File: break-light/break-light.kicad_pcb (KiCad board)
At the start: 2 copper layers, 70 x 70 mm, 78 parts, among them J1 Conn_01x03, J10 Conn_01x08, J11 Conn_01x08, J13 Conn_01x08, J14 Conn_01x08, J15 Conn_01x08, J16 Conn_01x08, J17 Conn_01x08, J3 Conn_01x05, J4 Conn_01x05, J9 Conn_01x08, SW1 SW_SPST, SW2 SW_SPST, U1 STM32F103C8Tx, U2 SN65HVD256D, U4 AP2204K-ADJ, U5 AP63200WU, U6 MAX7219CNG, U7 MAX7219CNG, U8 MAX7219CNG, U9 MAX7219CNG, Y1 8M, Y2 32.768k

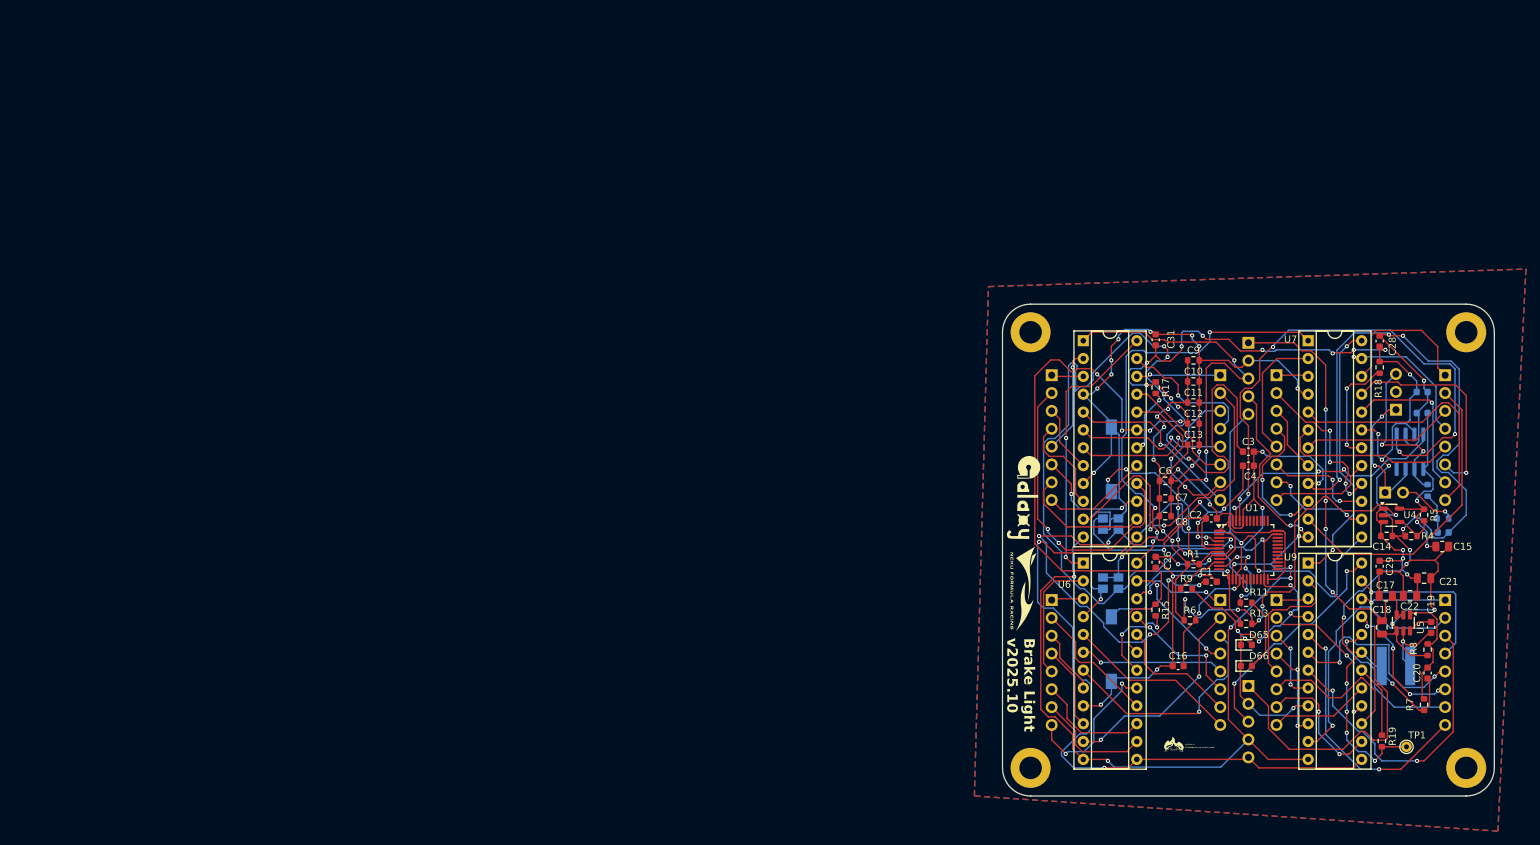
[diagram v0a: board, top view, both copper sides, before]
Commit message: fix: re-layout with 4 layers board
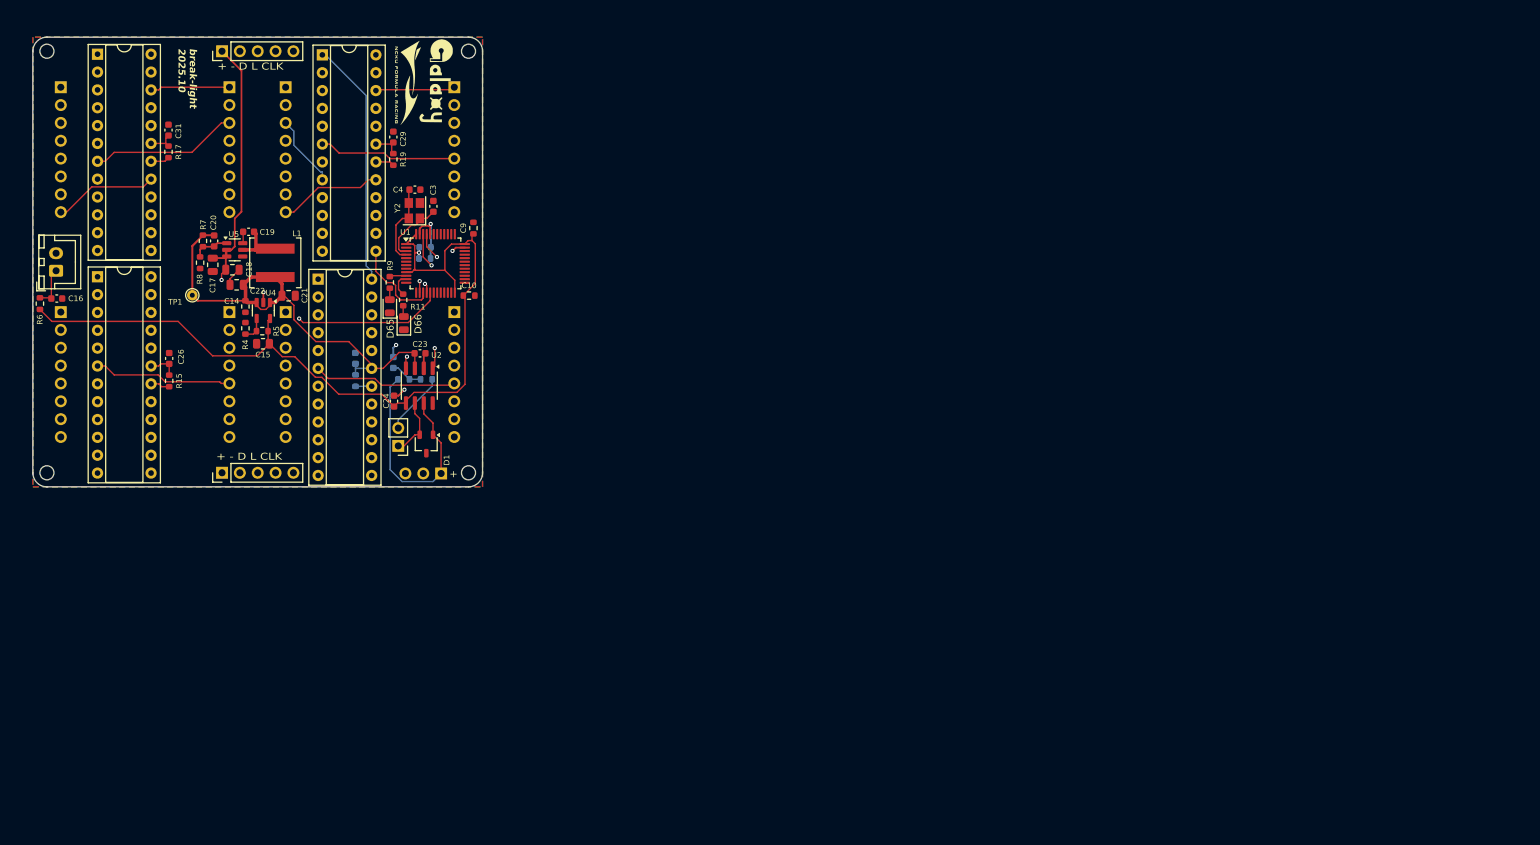
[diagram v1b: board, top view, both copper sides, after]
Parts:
- removed C1, C2: 20p, Capacitor_SMD:C_0603_1608Metric
- removed C12, C6, C8: 100n, Resistor_SMD:R_0603_1608Metric
- removed C7: 1u, Resistor_SMD:R_0603_1608Metric
- removed G***: LOGO, graph:shark
- removed H1, H2, H3, H4: MountingHole_Pad, MountingHole:MountingHole_3.2mm_M3_ISO7380_Pad
- removed R1, R13: 10k, Resistor_SMD:R_0603_1608Metric
- removed SW1, SW2: SW_SPST, Button_Switch_SMD:SW_SPST_FSMSM
- removed Y1: 8M, Crystal:Crystal_SMD_SeikoEpson_FA238-4Pin_3.2x2.5mm
- added D1: DESD2CAN2SOQ, Package_TO_SOT_SMD:TSOT-23, F.Cu at (75.0, 76.9)
- added J2: BSPD_IN, Connector_JST:JST_XH_B2B-XH-A_1x02_P2.50mm_Vertical, F.Cu at (22.3, 52.2)
- C11, C13, C28, R18: moved to B.Cu
- C23, C24, J3, J4, JP1, L1, U2, Y2: moved to F.Cu
- D65, D66: footprint LED_SMD:LED_0603_1608Metric -> LED_SMD:LED_0805_2012Metric
- moved R7 185.9 mm to (43.2, 48.0), turned to -90 degrees
- moved TP1 184.4 mm to (41.7, 55.7)
- moved C20 183.3 mm to (44.8, 48.0), turned to -90 degrees
- moved R8 183.2 mm to (42.8, 51.1)
- moved C19 177.5 mm to (49.7, 46.7), turned to 180 degrees
- moved U5 174.6 mm to (47.7, 49.3), turned to 0 degrees
- moved C17 173.5 mm to (44.6, 51.4), turned to -90 degrees
- moved C22 172.8 mm to (48.0, 54.2)
- moved J4 171.8 mm to (45.9, 21.0), turned to 90 degrees
- moved C18 171.3 mm to (47.4, 52.1), turned to 0 degrees
- moved C15 170.3 mm to (51.8, 62.6), turned to 180 degrees
- moved R6 169.8 mm to (20.0, 56.9), turned to 90 degrees
- moved L1 169.5 mm to (53.5, 51.1), turned to -90 degrees
- moved R4 168.5 mm to (49.2, 60.4), turned to -90 degrees
- moved C16 168.0 mm to (22.4, 56.2), turned to 180 degrees
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- renumbered G*** to G1, G*** to G2
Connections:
- JP1 pad 1: CAN+ -> CAN-
- R3 pad 2: CAN- -> CAN+
- U1 pad 1: +3.3V -> +3V3
- U1 pad 13: Net-(SW2-A) -> unconnected-(U1-PA3-Pad13)
- U1 pad 24: +3.3V -> +3V3
- U1 pad 36: +3.3V -> +3V3
- U1 pad 48: +3.3V -> +3V3
- U1 pad 5: /RCC_OSC_IN -> unconnected-(U1-PD0-Pad5)
- U1 pad 6: /RCC_OSC_OUT -> unconnected-(U1-PD1-Pad6)
- U1 pad 7: Net-(SW1-B) -> unconnected-(U1-NRST-Pad7)
- U1 pad 9: +3.3V -> +3V3
- U2 pad 8: unconnected-(U2-S-Pad8) -> GND
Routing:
- net GND: track 446.7 -> 21.1 mm, vias 38 -> 5
- net /LSE_IN: track 142.3 -> 9.46 mm, vias 4 -> 0
- net +5V: track 275.1 -> 160.6 mm, vias 28 -> 0
- net /RCC_OSC_IN: track 69.0 -> 0.00 mm, vias 6 -> 0
- net CAN_TX: track 79.7 -> 19.9 mm, vias 5 -> 2
- net BSPD_IN: track 17.3 -> 61.9 mm, vias 2 -> 1
- net DOUT2: track 62.6 -> 25.2 mm, vias 4 -> 0
- net VDC: track 106.8 -> 71.6 mm, vias 4 -> 1
- net Net-(SW2-A): track 29.5 -> 0.00 mm, vias 1 -> 0
- net /RCC_OSC_OUT: track 29.2 -> 0.00 mm, vias 1 -> 0
- net Net-(SW1-B): track 28.9 -> 0.00 mm, vias 3 -> 0
- net /LSE_OUT: track 39.1 -> 11.7 mm, vias 6 -> 0
- net +3.3V: track 26.9 -> 0.00 mm
- net COL1_1: track 43.7 -> 19.3 mm, vias 2 -> 0
- net DIN: track 78.3 -> 102.4 mm, vias 7 -> 1
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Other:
- board size 70 x 70 mm -> 64 x 64 mm
- copper layers 2 -> 4
- board text added: "+"
- board text added: "+ - D L CLK"
- board text added: "break-light 2025.10"
- board text removed: "Brake Light v2025.10"

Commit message: v2025.10
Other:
- board text added: "brake-light 2025.10"
- board text removed: "break-light 2025.10"
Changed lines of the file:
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@@
     (effects (font (size 1 1) (thickness 0.1)) (justify left bottom))
   )
-  (gr_text "break-light\n2025.10" (at 39.6 20.6 -90) (layer "F.SilkS")
+  (gr_text "brake-light\n2025.10" (at 39.6 20.6 270) (layer "F.SilkS")
     (effects (font (size 1 1) (thickness 0.2) bold italic) (justify left bottom))
   )

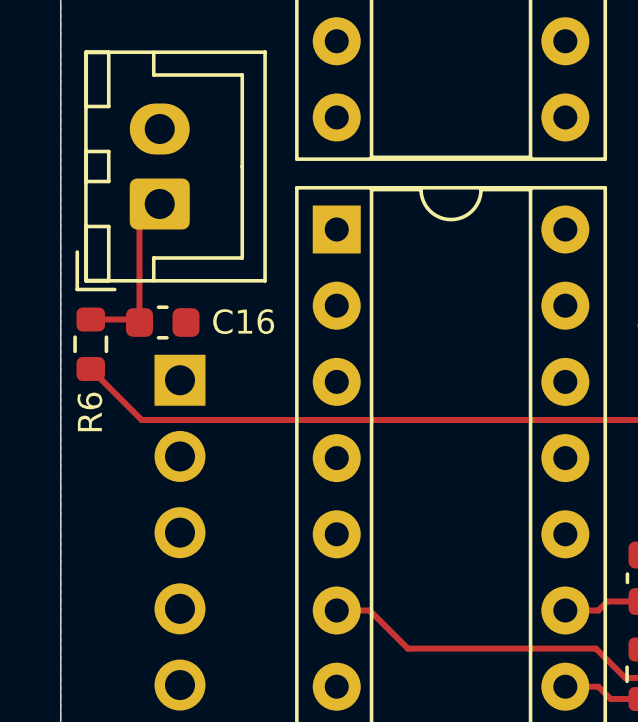
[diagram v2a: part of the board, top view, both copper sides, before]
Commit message: feat: add RC filter for brake light
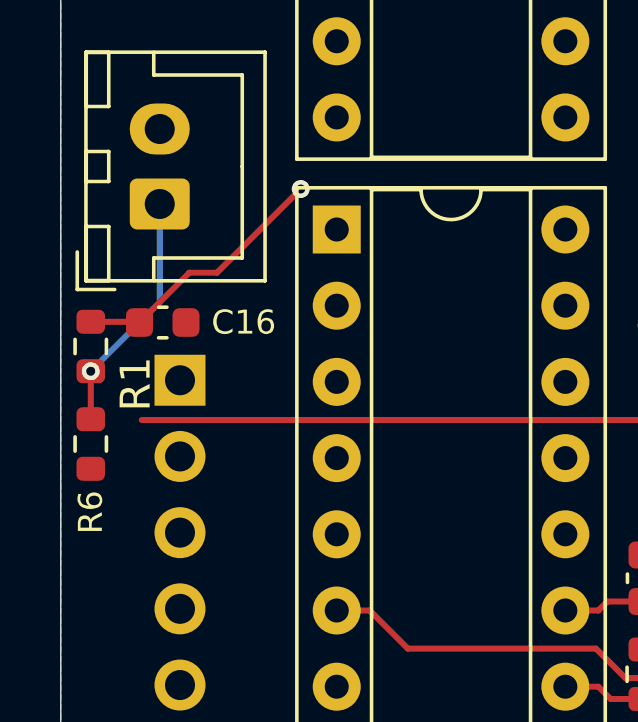
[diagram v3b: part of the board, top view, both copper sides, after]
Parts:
- added R1: 10k, Resistor_SMD:R_0603_1608Metric, F.Cu at (20.0, 57.0)
- moved R6 3.33 mm to (20.0, 60.2)
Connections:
- C16 pad 2: BSPD_IN -> Net-(U1-PA6)
- J2 pad 1: BSPD_IN -> BSE_IN
- R6 pad 1: +3V3 -> GND
- R6 pad 2: BSPD_IN -> BSE_IN
- U1 pad 16: BSPD_IN -> Net-(U1-PA6)
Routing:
- net BSPD_IN: track 61.9 -> 0.00 mm, vias 1 -> 0
- net Net-(U1-PA6): track 0.00 -> 59.3 mm, vias 0 -> 2
- net BSE_IN: track 0.00 -> 9.08 mm, vias 0 -> 1
- net +3V3: track 121.2 -> 118.8 mm

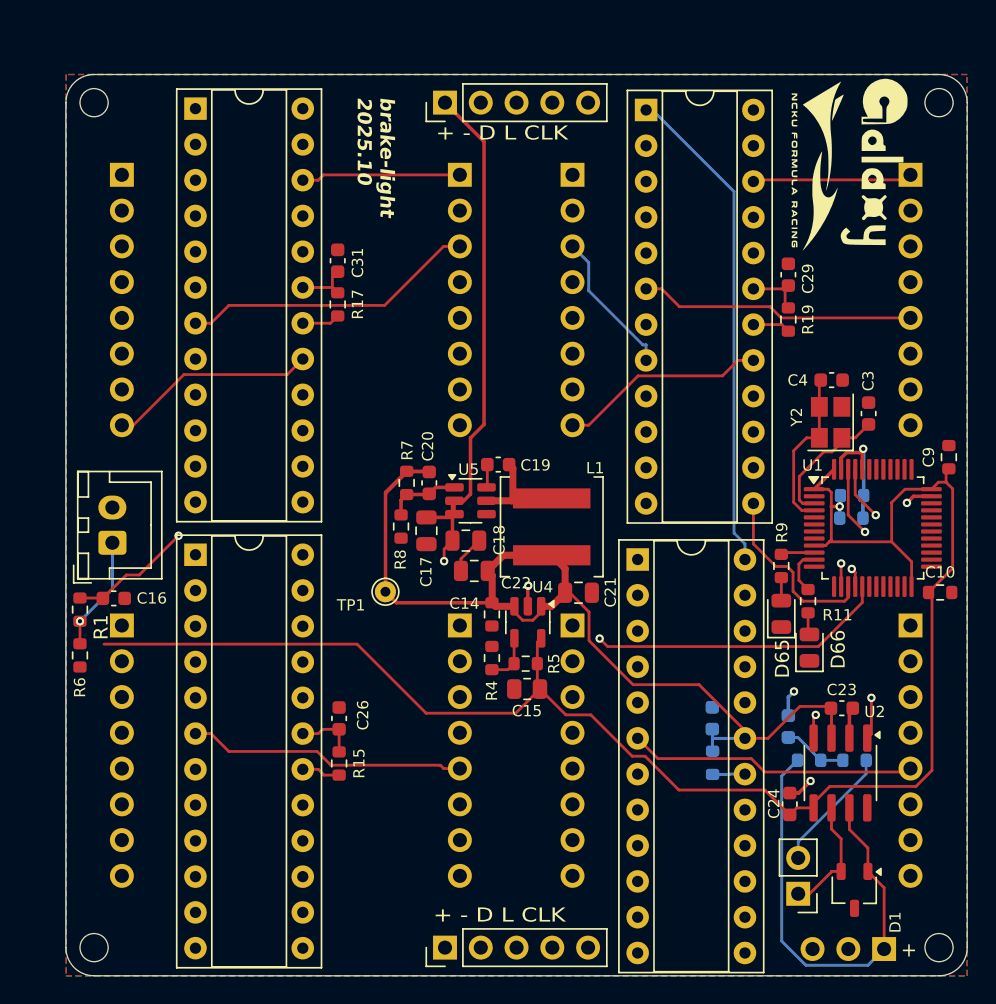
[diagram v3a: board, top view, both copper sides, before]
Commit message: feat: flip one side of the LED matrix
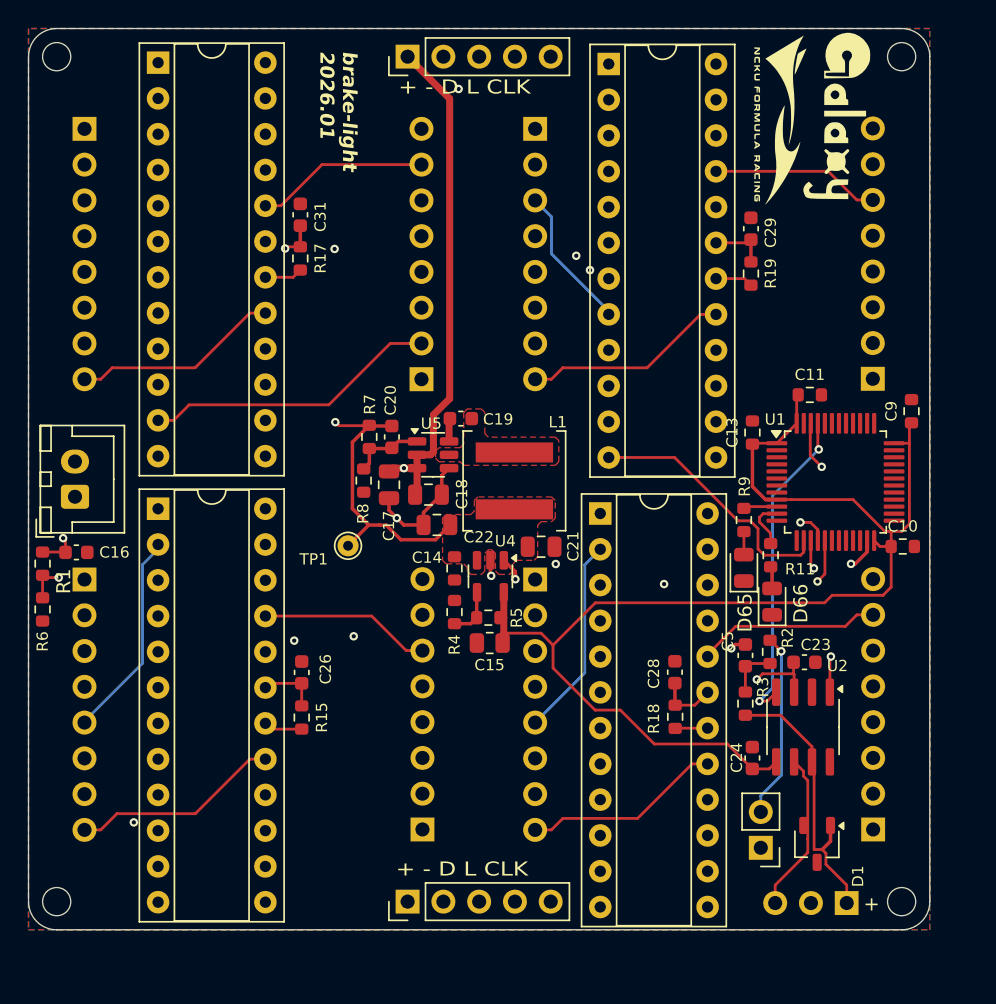
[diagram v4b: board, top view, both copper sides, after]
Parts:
- removed C3, C4: 20p, Capacitor_SMD:C_0603_1608Metric
- removed Y2: 32.768k, Crystal:Crystal_SMD_SeikoEpson_FA238-4Pin_3.2x2.5mm
- C11, C13, C28, C5, R18, R2, R3: moved to F.Cu
- moved J14 14.8 mm to (44.2, 40.6), turned to 0 degrees
- moved J17 14.7 mm to (76.3, 40.6), turned to 0 degrees
- moved J15 14.7 mm to (44.3, 72.6), turned to 0 degrees
- moved J16 14.7 mm to (76.3, 72.6), turned to 0 degrees
- moved R2 9.76 mm to (69.0, 60.0), turned to -90 degrees
- moved C13 9.29 mm to (67.8, 44.4), turned to 90 degrees
- moved C11 7.75 mm to (71.8, 41.8)
- moved R3 6.06 mm to (67.2, 63.7), turned to -90 degrees
- moved C5 5.90 mm to (67.2, 60.2)
- moved C29 4.21 mm to (67.6, 29.9)
- moved C10 4.21 mm to (78.4, 52.5)
- moved C14 4.21 mm to (46.6, 54.1)
- moved C15 4.21 mm to (49.1, 59.4)
- moved C17 4.21 mm to (41.9, 48.1)
- moved C18 4.21 mm to (44.7, 48.8)
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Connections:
- U1 pad 3: /LSE_IN -> unconnected-(U1-PC14-Pad3)
- U1 pad 4: /LSE_OUT -> unconnected-(U1-PC15-Pad4)
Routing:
- net +5V: track 160.6 -> 129.6 mm, vias 0 -> 10
- net +3V3: track 118.8 -> 89.5 mm, vias 1 -> 0
- net ROW1_1: track 38.1 -> 21.0 mm
- net ROW4_1: track 38.3 -> 22.0 mm
- net CAN+: track 32.8 -> 20.1 mm
- net /LSE_OUT: track 11.7 -> 0.00 mm
- net COL2_7: track 11.4 -> 22.5 mm
- net COL1_7: track 11.3 -> 22.2 mm
- net COL4_7: track 11.4 -> 21.9 mm
- net COL3_7: track 11.9 -> 22.2 mm
- net DIN: track 102.4 -> 112.1 mm, vias 1 -> 3
- net /LSE_IN: track 9.46 -> 0.00 mm
- net ROW1_2: track 28.1 -> 19.5 mm
- net GND: track 21.1 -> 13.1 mm, vias 5 -> 4
- net ROW3_1: track 30.4 -> 22.6 mm
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- added copper zone on F.Cu, net +5V
- added copper zone on F.Cu, net Net-(U5-SW)
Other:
- board text added: "brake-light 2026.01"
- board text removed: "brake-light 2025.10"

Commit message: fix: repair pin
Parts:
- added J5: Conn_01x03, Connector_PinHeader_2.54mm:PinHeader_1x03_P2.54mm_Vertical, F.Cu at (72.0, 36.6)
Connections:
- J10 pad 1: ROW3_4 -> COL3_7
- J10 pad 2: COL3_1 -> COL3_6
- J10 pad 3: ROW3_7 -> ROW3_1
- J10 pad 4: ROW3_5 -> COL3_0
- J10 pad 5: ROW3_0 -> ROW3_3
- J10 pad 7: COL3_0 -> COL3_3
- J10 pad 8: COL3_6 -> ROW3_0
- J11 pad 1: ROW4_4 -> COL4_7
- J11 pad 2: COL4_1 -> COL4_6
- J11 pad 3: ROW4_7 -> ROW4_1
- J11 pad 4: ROW4_5 -> COL4_0
- J11 pad 5: ROW4_0 -> ROW4_3
- J11 pad 7: COL4_0 -> COL4_3
- J11 pad 8: COL4_6 -> ROW4_0
- J13 pad 1: ROW1_4 -> COL1_7
- J13 pad 2: COL1_1 -> COL1_6
- J13 pad 3: ROW1_7 -> ROW1_1
- J13 pad 4: ROW1_5 -> COL1_0
- J13 pad 5: ROW1_0 -> ROW1_3
- J13 pad 7: COL1_0 -> COL1_3
- J13 pad 8: COL1_6 -> ROW1_0
- J14 pad 1: COL1_7 -> ROW1_2
- J14 pad 2: ROW1_1 -> ROW1_5
- J14 pad 3: ROW1_3 -> COL1_4
- J14 pad 4: COL1_3 -> ROW1_7
- J14 pad 5: ROW1_2 -> COL1_2
- J14 pad 6: COL1_4 -> COL1_1
- J14 pad 7: COL1_2 -> ROW1_6
- J14 pad 8: ROW1_6 -> ROW1_4
- J15 pad 1: COL2_7 -> ROW2_2
- J15 pad 2: ROW2_1 -> ROW2_5
- J15 pad 3: ROW2_3 -> COL2_4
- J15 pad 4: COL2_3 -> ROW2_7
- J15 pad 5: ROW2_2 -> COL2_2
- J15 pad 6: COL2_4 -> COL2_1
- J15 pad 7: COL2_2 -> ROW2_6
- J15 pad 8: ROW2_6 -> ROW2_4
- J16 pad 1: COL3_7 -> ROW3_2
- J16 pad 2: ROW3_1 -> ROW3_5
- J16 pad 3: ROW3_3 -> COL3_4
- J16 pad 4: COL3_3 -> ROW3_7
- J16 pad 5: ROW3_2 -> COL3_2
- J16 pad 6: COL3_4 -> COL3_1
- J16 pad 7: COL3_2 -> ROW3_6
- J16 pad 8: ROW3_6 -> ROW3_4
- J17 pad 1: COL4_7 -> ROW4_2
- J17 pad 2: ROW4_1 -> ROW4_5
- J17 pad 3: ROW4_3 -> COL4_4
- J17 pad 4: COL4_3 -> ROW4_7
- J17 pad 5: ROW4_2 -> COL4_2
- J17 pad 6: COL4_4 -> COL4_1
- J17 pad 7: COL4_2 -> ROW4_6
- J17 pad 8: ROW4_6 -> ROW4_4
- J9 pad 1: ROW2_4 -> COL2_7
- J9 pad 2: COL2_1 -> COL2_6
- J9 pad 3: ROW2_7 -> ROW2_1
- J9 pad 4: ROW2_5 -> COL2_0
- J9 pad 5: ROW2_0 -> ROW2_3
- J9 pad 7: COL2_0 -> COL2_3
- J9 pad 8: COL2_6 -> ROW2_0
- U1 pad 34: unconnected-(U1-PA13-Pad34) -> SWDIO
- U1 pad 37: unconnected-(U1-PA14-Pad37) -> SWCLK
- U6 pad 10: ROW2_5 -> COL2_5
- U6 pad 11: ROW2_1 -> COL2_1
- U6 pad 14: COL2_0 -> ROW2_0
- U6 pad 15: COL2_5 -> ROW2_5
- U6 pad 16: COL2_1 -> ROW2_1
- U6 pad 17: COL2_6 -> ROW2_6
- U6 pad 2: ROW2_0 -> COL2_0
- U6 pad 20: COL2_2 -> ROW2_2
- U6 pad 21: COL2_4 -> ROW2_4
- U6 pad 22: COL2_7 -> ROW2_7
- U6 pad 23: COL2_3 -> ROW2_3
- U6 pad 3: ROW2_4 -> COL2_4
- U6 pad 5: ROW2_6 -> COL2_6
- U6 pad 6: ROW2_2 -> COL2_2
- U6 pad 7: ROW2_3 -> COL2_3
- U6 pad 8: ROW2_7 -> COL2_7
- U7 pad 10: ROW3_5 -> COL3_5
- U7 pad 11: ROW3_1 -> COL3_1
- U7 pad 14: COL3_0 -> ROW3_0
- U7 pad 15: COL3_5 -> ROW3_5
- U7 pad 16: COL3_1 -> ROW3_1
- U7 pad 17: COL3_6 -> ROW3_6
- U7 pad 2: ROW3_0 -> COL3_0
- U7 pad 20: COL3_2 -> ROW3_2
- U7 pad 21: COL3_4 -> ROW3_4
- U7 pad 22: COL3_7 -> ROW3_7
- U7 pad 23: COL3_3 -> ROW3_3
- U7 pad 3: ROW3_4 -> COL3_4
- U7 pad 5: ROW3_6 -> COL3_6
- U7 pad 6: ROW3_2 -> COL3_2
- U7 pad 7: ROW3_3 -> COL3_3
- U7 pad 8: ROW3_7 -> COL3_7
- U8 pad 10: ROW1_5 -> COL1_5
- U8 pad 11: ROW1_1 -> COL1_1
- U8 pad 14: COL1_0 -> ROW1_0
- U8 pad 15: COL1_5 -> ROW1_5
- U8 pad 16: COL1_1 -> ROW1_1
- U8 pad 17: COL1_6 -> ROW1_6
- U8 pad 2: ROW1_0 -> COL1_0
- U8 pad 20: COL1_2 -> ROW1_2
- U8 pad 21: COL1_4 -> ROW1_4
- U8 pad 22: COL1_7 -> ROW1_7
- U8 pad 23: COL1_3 -> ROW1_3
- U8 pad 3: ROW1_4 -> COL1_4
- U8 pad 5: ROW1_6 -> COL1_6
- U8 pad 6: ROW1_2 -> COL1_2
- U8 pad 7: ROW1_3 -> COL1_3
- U8 pad 8: ROW1_7 -> COL1_7
- U9 pad 10: ROW4_5 -> COL4_5
- U9 pad 11: ROW4_1 -> COL4_1
- U9 pad 14: COL4_0 -> ROW4_0
- U9 pad 15: COL4_5 -> ROW4_5
- U9 pad 16: COL4_1 -> ROW4_1
- U9 pad 17: COL4_6 -> ROW4_6
- U9 pad 2: ROW4_0 -> COL4_0
- U9 pad 20: COL4_2 -> ROW4_2
- U9 pad 21: COL4_4 -> ROW4_4
- U9 pad 22: COL4_7 -> ROW4_7
- U9 pad 23: COL4_3 -> ROW4_3
- U9 pad 3: ROW4_4 -> COL4_4
- U9 pad 5: ROW4_6 -> COL4_6
- U9 pad 6: ROW4_2 -> COL4_2
- U9 pad 7: ROW4_3 -> COL4_3
- U9 pad 8: ROW4_7 -> COL4_7
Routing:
- net COL2_4: track 12.2 -> 29.0 mm
- net COL4_4: track 12.0 -> 28.7 mm
- net COL1_4: track 12.0 -> 28.4 mm, vias 0 -> 1
- net COL3_4: track 12.6 -> 28.0 mm, vias 0 -> 1
- net SWCLK: track 0.00 -> 14.5 mm
- net COL4_1: track 23.0 -> 37.0 mm, vias 0 -> 1
- net COL2_1: track 22.0 -> 36.0 mm, vias 0 -> 1
- net SWDIO: track 0.00 -> 12.7 mm, vias 0 -> 2
- net COL3_1: track 20.4 -> 32.9 mm, vias 0 -> 1
- net GND: track 13.1 -> 23.6 mm, vias 4 -> 5
- net COL1_1: track 21.0 -> 31.5 mm, vias 0 -> 1
- net COL3_3: track 17.8 -> 7.38 mm
- net COL2_3: track 17.4 -> 7.98 mm
- net COL1_3: track 17.1 -> 7.82 mm
- net COL4_3: track 16.8 -> 7.81 mm
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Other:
- board text added: "brake-light 2026.03"
- board text removed: "brake-light 2026.01"
